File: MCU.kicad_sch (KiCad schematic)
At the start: 2 parts, among them U6 ESP32-S3-WROOM-1-N16R8, U9 M24C01-WMN

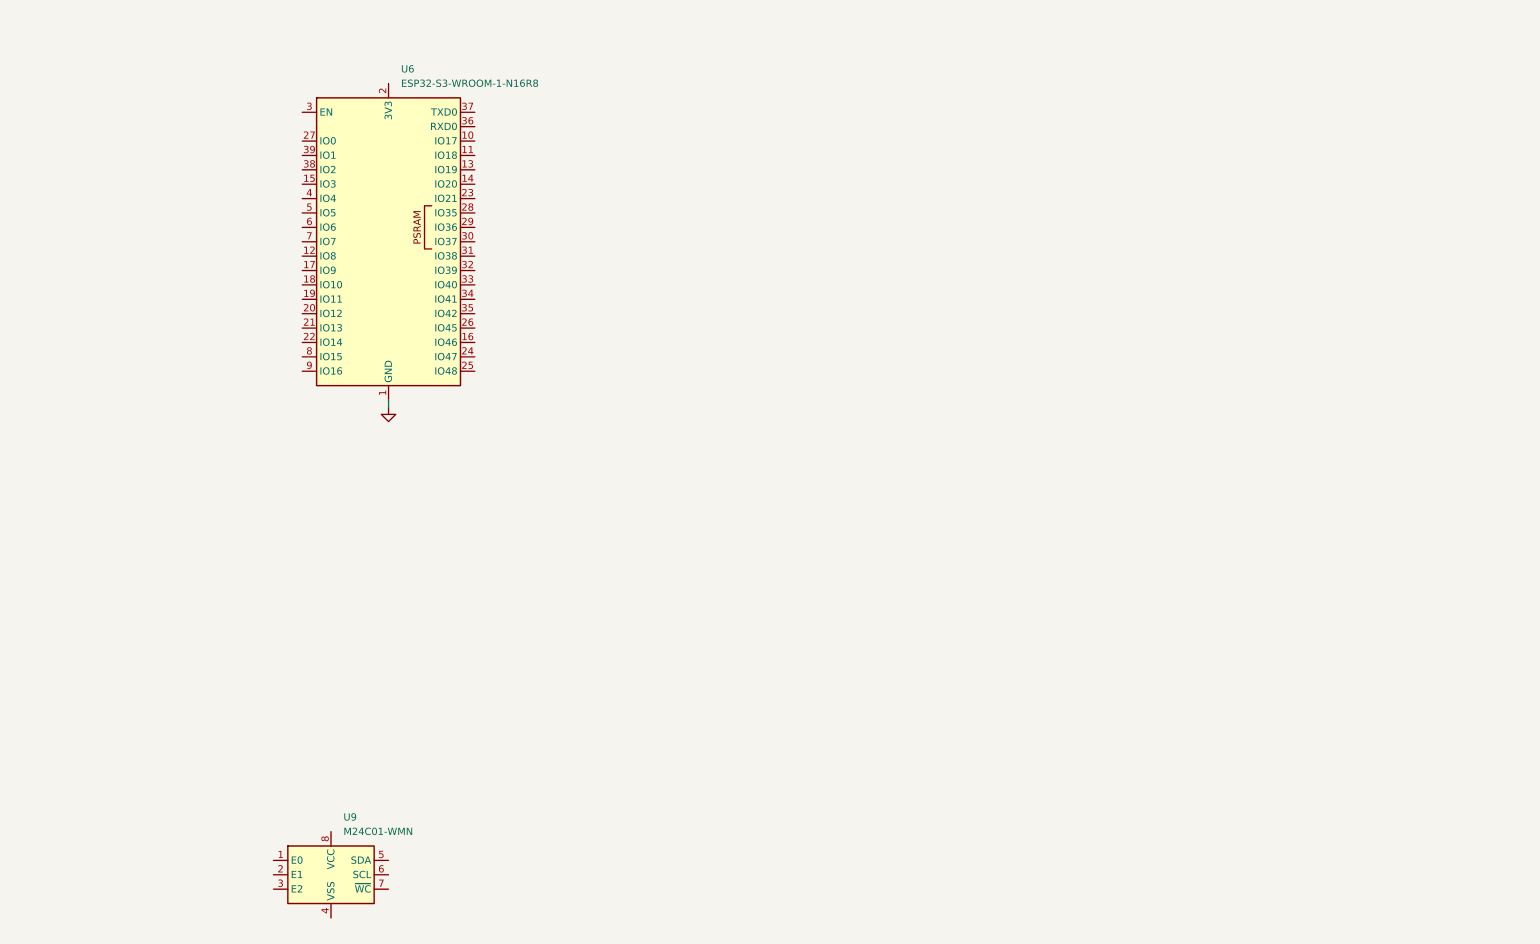
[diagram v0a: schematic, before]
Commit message: schematics mixer progress, mcu
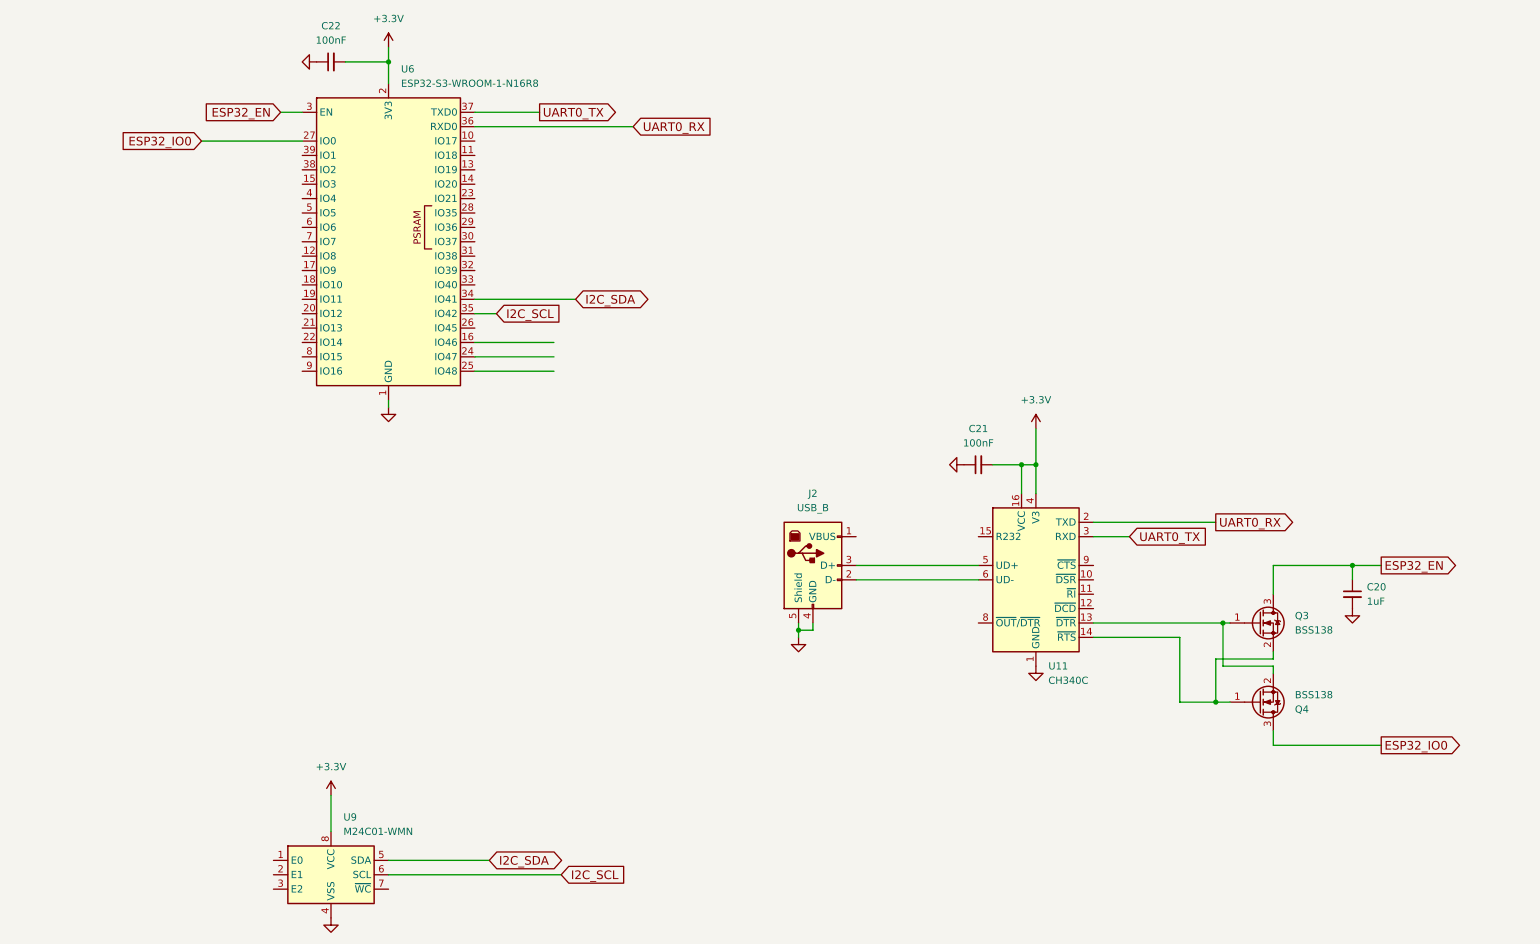
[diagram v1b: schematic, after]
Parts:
- added C20: 1uF, Capacitor_SMD:C_0603_1608Metric_Pad1.08x0.95mm_HandSolder, symbol Device:C_Small
- added C21, C22: 100nF, Capacitor_SMD:C_0603_1608Metric_Pad1.08x0.95mm_HandSolder, symbol Device:C_Small
- added J2: USB_B, Connector_USB:USB_B_OST_USB-B1HSxx_Horizontal, symbol Connector:USB_B
- added Q3, Q4: BSS138, Package_TO_SOT_SMD:SOT-23, symbol Transistor_FET:BSS138
- added U11: CH340C, Package_SO:SOIC-16_3.9x9.9mm_P1.27mm, symbol Interface_USB:CH340C
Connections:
- net GND: now also U9.4 (VSS), C20.2, C21.1, C22.1, J2.4 (GND), J2.5 (Shield), U11.1 (GND)
- net +3.3V: now reaches U6.2 (3V3)
- net +3.3V: now also U9.8 (VCC), C21.2, C22.2, U11.16 (VCC), U11.4 (V3)
- net ESP32_IO0: now reaches U6.27 (IO0)
- net ESP32_IO0: now also Q4.3 (D)
- net ESP32_EN: now reaches U6.3 (EN)
- net ESP32_EN: now also C20.1, Q3.3 (D)
- net I2C_SDA: now reaches U6.34 (IO41)
- net I2C_SDA: now also U9.5 (SDA)
- net I2C_SCL: now reaches U6.35 (IO42)
- net I2C_SCL: now also U9.6 (SCL)
- net UART0_RX: now reaches U6.36 (RXD0)
- net UART0_RX: now also U11.2 (TXD)
- net UART0_TX: now reaches U6.37 (TXD0)
- net UART0_TX: now also U11.3 (RXD)
- new net: Q3.2 (S), Q4.1 (G), U11.14 (~{RTS})
- new net: Q3.1 (G), Q4.2 (S), U11.13 (~{DTR})
- new net: J2.2 (D-), U11.6 (UD-)
- new net: J2.3 (D+), U11.5 (UD+)

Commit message: add BPF, add Firmware
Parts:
- added J3: Program_USB_JTAG, Connector_PinHeader_2.54mm:PinHeader_1x03_P2.54mm_Vertical, symbol Connector_Generic:Conn_01x03
- Q3: JLCPCB (none) -> C82045
- U11: JLCPCB (none) -> C7464026
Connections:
- net GND: now also U9.1 (E0), U9.2 (E1), U9.3 (E2), J3.3 (Pin_3)
- net I2C_SCL: now also U6.34 (IO41); no longer U6.35 (IO42)
- net I2C_SDA: now also U6.35 (IO42); no longer U6.34 (IO41)
- net KEYBOARD3: now reaches U6.12 (IO8)
- net USB_D-: now reaches U6.13 (IO19)
- net USB_D-: now also J3.1 (Pin_1)
- net USB_D+: now reaches U6.14 (IO20)
- net USB_D+: now also J3.2 (Pin_2)
- net LCD1602_IO3: now reaches U6.15 (IO3)
- net 74HC4053_RX_TX: now reaches U6.16 (IO46)
- net KEYBOARD4: now reaches U6.17 (IO9)
- net ENCODER_A: now reaches U6.18 (IO10)
- net ENCODER_B: now reaches U6.19 (IO11)
- net PREAMP: now reaches U6.24 (IO47)
- net EEPROM_WP: now reaches U6.25 (IO48)
- net EEPROM_WP: now also U9.7 (~{WC})
- net LCD1602_IO2: now reaches U6.38 (IO2)
- net LCD1602_IO1: now reaches U6.39 (IO1)
- net CW_Key_DOT: now reaches U6.4 (IO4)
- net CW_Key_DACH: now reaches U6.5 (IO5)
- net KEYBOARD1: now reaches U6.6 (IO6)
- net KEYBOARD2: now reaches U6.7 (IO7)

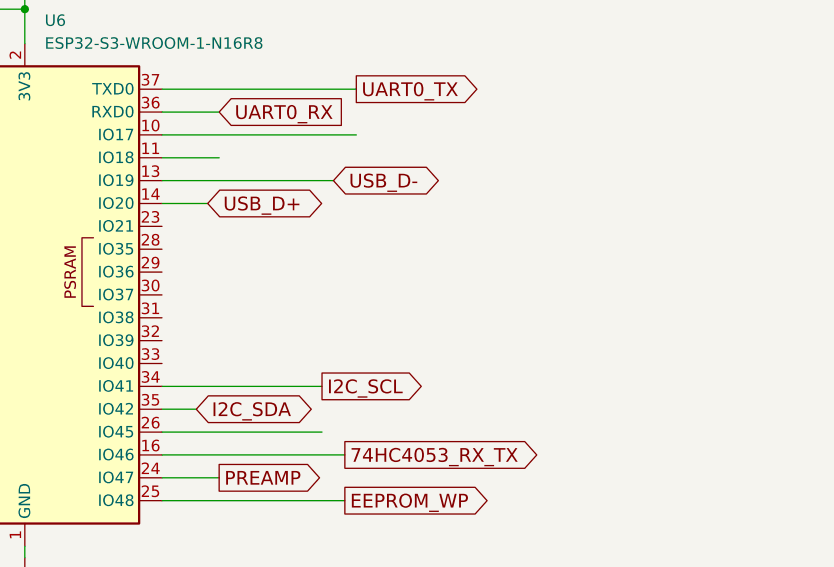
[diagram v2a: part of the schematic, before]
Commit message: add custom footprints, progress on schema and PCB
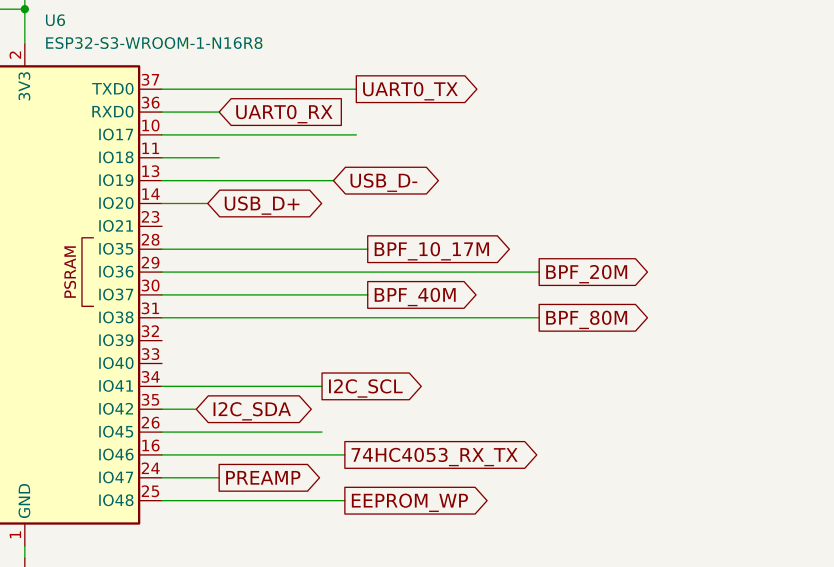
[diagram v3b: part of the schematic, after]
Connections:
- net BPF_10_17M: now reaches U6.28 (IO35)
- net BPF_20M: now reaches U6.29 (IO36)
- net BPF_40M: now reaches U6.30 (IO37)
- net BPF_80M: now reaches U6.31 (IO38)
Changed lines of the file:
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@@
+	(wire
+		(pts
+			(xy 95.25 60.96) (xy 118.11 60.96)
+		)
+		(stroke
+			(width 0)
+			(type default)
+		)
+	)
 	(wire
 		(pts
@@
 	(wire
 		(pts
+			(xy 95.25 63.5) (xy 137.16 63.5)
+		)
+		(stroke
+			(width 0)
+			(type default)
+		)
+	)
+	(wire
+		(pts
 			(xy 80.01 90.17) (xy 80.01 88.9)
 		)
@@
 	(wire
 		(pts
+			(xy 95.25 58.42) (xy 137.16 58.42)
+		)
+		(stroke
+			(width 0)
+			(type default)
+		)
+	)
+	(wire
+		(pts
 			(xy 80.01 29.21) (xy 80.01 33.02)
 		)
@@
 		(pts
 			(xy 236.22 149.86) (xy 255.27 149.86)
+		)
+		(stroke
+			(width 0)
+			(type default)
+		)
+	)
+	(wire
+		(pts
+			(xy 95.25 55.88) (xy 118.11 55.88)
 		)
 		(stroke
@@
 		)
 	)
+	(global_label "BPF_80M"
+		(shape output)
+		(at 137.16 63.5 0)
+		(fields_autoplaced yes)
+		(effects
+			(font
+				(size 1.524 1.524)
+			)
+			(justify left)
+		)
+		(property "Intersheetrefs" "${INTERSHEET_REFS}"
+			(at 150.1167 63.5 0)
+			(effects
+				(font
+					(size 1.27 1.27)
+				)
+				(justify left)
+				(hide yes)
+			)
+		)
+	)
 	(global_label "UART0_RX"
 		(shape output)
@@
 		)
 	)
+	(global_label "BPF_10_17M"
+		(shape output)
+		(at 118.11 55.88 0)
+		(fields_autoplaced yes)
+		(effects
+			(font
+				(size 1.524 1.524)
+			)
+			(justify left)
+		)
+		(property "Intersheetrefs" "${INTERSHEET_REFS}"
+			(at 135.1306 55.88 0)
+			(effects
+				(font
+					(size 1.27 1.27)
+				)
+				(justify left)
+				(hide yes)
+			)
+		)
+	)
 	(global_label "ESP32_EN"
 		(shape input)
@@
 		)
 	)
+	(global_label "BPF_40M"
+		(shape output)
+		(at 118.11 60.96 0)
+		(fields_autoplaced yes)
+		(effects
+			(font
+				(size 1.524 1.524)
+			)
+			(justify left)
+		)
+		(property "Intersheetrefs" "${INTERSHEET_REFS}"
+			(at 131.0667 60.96 0)
+			(effects
+				(font
+					(size 1.27 1.27)
+				)
+				(justify left)
+				(hide yes)
+			)
+		)
+	)
 	(global_label "74HC4053_RX_TX"
 		(shape output)
@@
 				(hide yes)
 			)
+		)
+	)
+	(global_label "BPF_20M"
+		(shape output)
+		(at 137.16 58.42 0)
+		(fields_autoplaced yes)
+		(effects
+			(font
+				(size 1.524 1.524)
+			)
+			(justify left)
+		)
+		(property "Intersheetrefs" "${INTERSHEET_REFS}"
+			(at 150.1167 58.42 0)
+			(effects
+				(font
+					(size 1.27 1.27)
+				)
+				(justify left)
+				(hide yes)
+			)

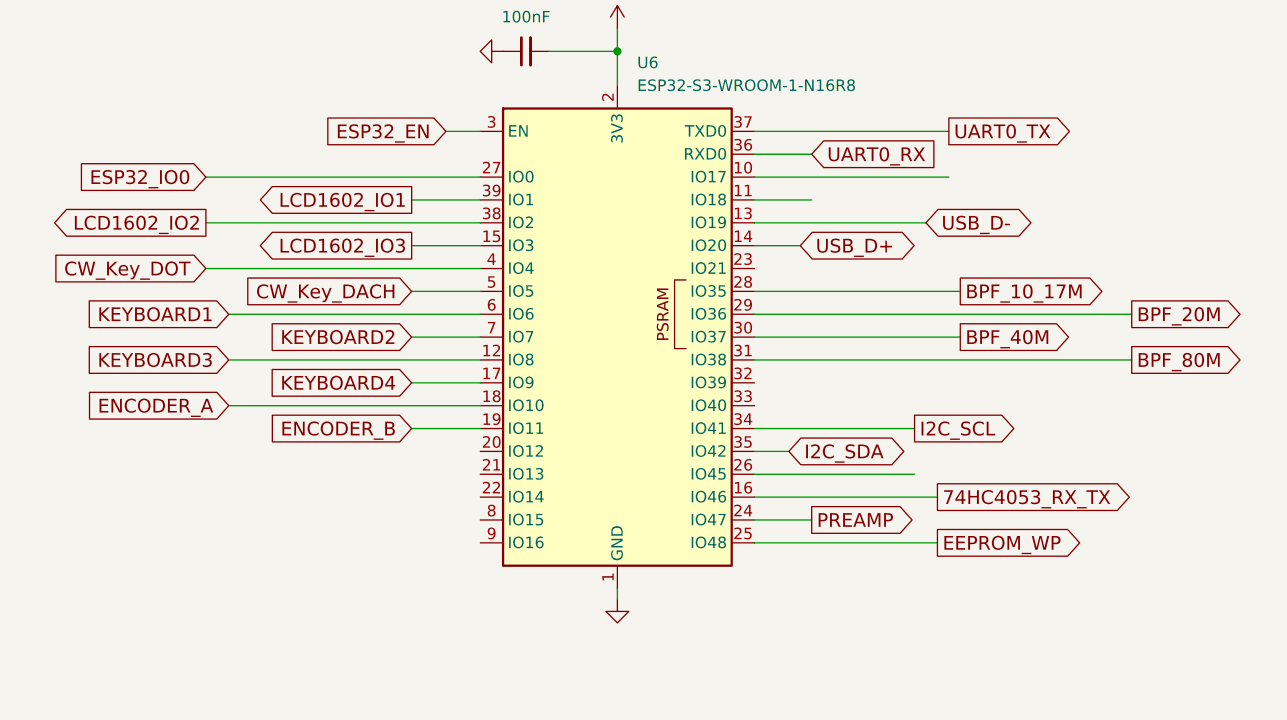
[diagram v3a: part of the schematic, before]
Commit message: progress in PCB, schematics some footprints are still missing
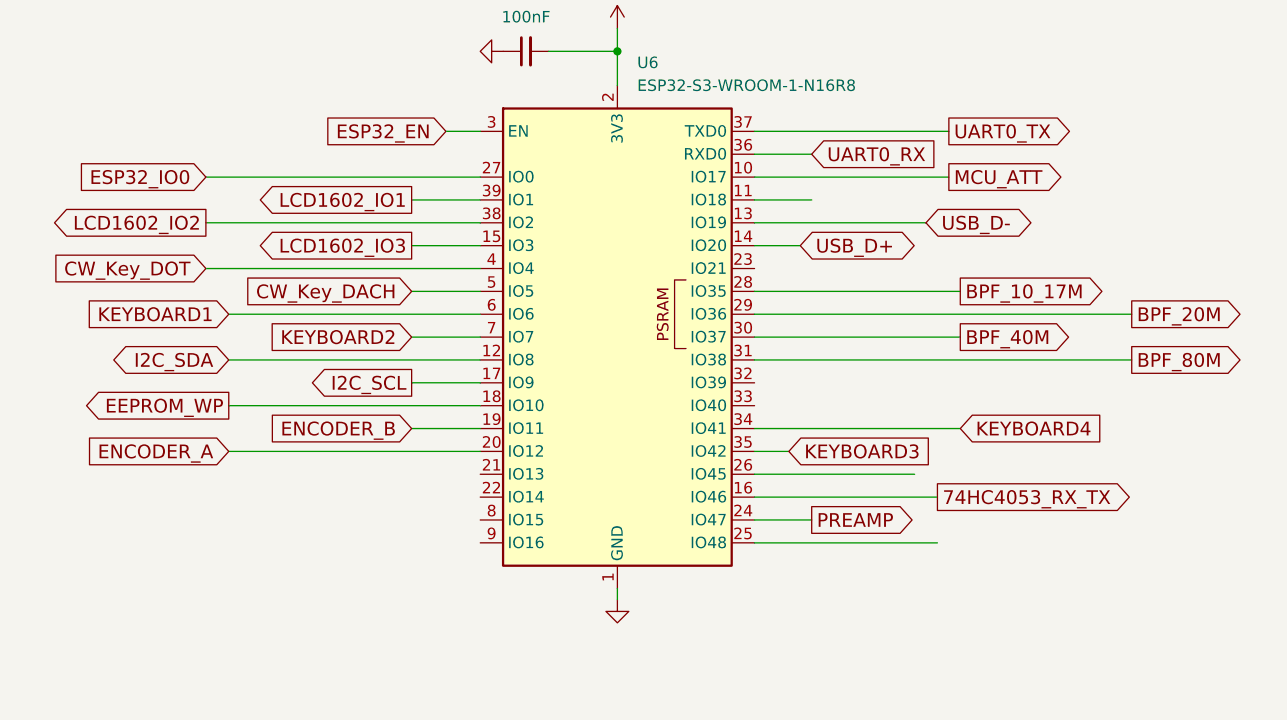
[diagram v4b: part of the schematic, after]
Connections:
- net EEPROM_WP: now also U6.18 (IO10); no longer U6.25 (IO48)
- net ENCODER_A: now also U6.20 (IO12); no longer U6.18 (IO10)
- net I2C_SCL: now also U6.17 (IO9); no longer U6.34 (IO41)
- net I2C_SDA: now also U6.12 (IO8); no longer U6.35 (IO42)
- net KEYBOARD3: now also U6.35 (IO42); no longer U6.12 (IO8)
- net KEYBOARD4: now also U6.34 (IO41); no longer U6.17 (IO9)
- net MCU_ATT: now reaches U6.10 (IO17)
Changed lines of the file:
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@@
+	(wire
+		(pts
+			(xy 36.83 73.66) (xy 64.77 73.66)
+		)
+		(stroke
+			(width 0)
+			(type default)
+		)
+	)
 	(wire
 		(pts
@@
 	(wire
 		(pts
-			(xy 95.25 71.12) (xy 113.03 71.12)
+			(xy 95.25 71.12) (xy 118.11 71.12)
 		)
 		(stroke
@@
 	(global_label "ENCODER_A"
 		(shape input)
-		(at 36.83 68.58 180)
-		(fields_autoplaced yes)
-		(effects
-			(font
-				(size 1.524 1.524)
-			)
-			(justify right)
-		)
-		(property "Intersheetrefs" "${INTERSHEET_REFS}"
-			(at 21.0428 68.58 0)
+		(at 36.83 73.66 180)
+		(fields_autoplaced yes)
+		(effects
+			(font
+				(size 1.524 1.524)
+			)
+			(justify right)
+		)
+		(property "Intersheetrefs" "${INTERSHEET_REFS}"
+			(at 21.0428 73.66 0)
 			(effects
 				(font
@@
 	(global_label "KEYBOARD4"
 		(shape input)
-		(at 57.15 66.04 180)
-		(fields_autoplaced yes)
-		(effects
-			(font
-				(size 1.524 1.524)
-			)
-			(justify right)
-		)
-		(property "Intersheetrefs" "${INTERSHEET_REFS}"
-			(at 41.2177 66.04 0)
-			(effects
-				(font
-					(size 1.27 1.27)
-				)
-				(justify right)
+		(at 118.11 71.12 0)
+		(fields_autoplaced yes)
+		(effects
+			(font
+				(size 1.524 1.524)
+			)
+			(justify left)
+		)
+		(property "Intersheetrefs" "${INTERSHEET_REFS}"
+			(at 134.0423 71.12 0)
+			(effects
+				(font
+					(size 1.27 1.27)
+				)
+				(justify left)
 				(hide yes)
 			)
@@
 	(global_label "I2C_SDA"
 		(shape bidirectional)
-		(at 99.06 73.66 0)
-		(fields_autoplaced yes)
-		(effects
-			(font
-				(size 1.524 1.524)
-			)
-			(justify left)
-		)
-		(property "Intersheetrefs" "${INTERSHEET_REFS}"
-			(at 112.1437 73.66 0)
-			(effects
-				(font
-					(size 1.27 1.27)
-				)
-				(justify left)
+		(at 36.83 63.5 180)
+		(fields_autoplaced yes)
+		(effects
+			(font
+				(size 1.524 1.524)
+			)
+			(justify right)
+		)
+		(property "Intersheetrefs" "${INTERSHEET_REFS}"
+			(at 23.7463 63.5 0)
+			(effects
+				(font
+					(size 1.27 1.27)
+				)
+				(justify right)
 				(hide yes)
 			)
@@
 	(global_label "KEYBOARD3"
 		(shape input)
-		(at 36.83 63.5 180)
-		(fields_autoplaced yes)
-		(effects
-			(font
-				(size 1.524 1.524)
-			)
-			(justify right)
-		)
-		(property "Intersheetrefs" "${INTERSHEET_REFS}"
-			(at 20.8977 63.5 0)
-			(effects
-				(font
-					(size 1.27 1.27)
-				)
-				(justify right)
+		(at 99.06 73.66 0)
+		(fields_autoplaced yes)
+		(effects
+			(font
+				(size 1.524 1.524)
+			)
+			(justify left)
+		)
+		(property "Intersheetrefs" "${INTERSHEET_REFS}"
+			(at 114.9923 73.66 0)
+			(effects
+				(font
+					(size 1.27 1.27)
+				)
+				(justify left)
 				(hide yes)
 			)
@@
 	(global_label "EEPROM_WP"
 		(shape output)
-		(at 115.57 83.82 0)
-		(fields_autoplaced yes)
-		(effects
-			(font
-				(size 1.524 1.524)
-			)
-			(justify left)
-		)
-		(property "Intersheetrefs" "${INTERSHEET_REFS}"
-			(at 131.9377 83.82 0)
-			(effects
-				(font
-					(size 1.27 1.27)
-				)
-				(justify left)
+		(at 36.83 68.58 180)
+		(fields_autoplaced yes)
+		(effects
+			(font
+				(size 1.524 1.524)
+			)
+			(justify right)
+		)
+		(property "Intersheetrefs" "${INTERSHEET_REFS}"
+			(at 20.4623 68.58 0)
+			(effects
+				(font
+					(size 1.27 1.27)
+				)
+				(justify right)
 				(hide yes)
 			)
@@
 	(global_label "I2C_SCL"
 		(shape output)
-		(at 113.03 71.12 0)
-		(fields_autoplaced yes)
-		(effects
-			(font
-				(size 1.524 1.524)
-			)
-			(justify left)
-		)
-		(property "Intersheetrefs" "${INTERSHEET_REFS}"
-			(at 124.8981 71.12 0)
-			(effects
-				(font
-					(size 1.27 1.27)
-				)
-				(justify left)
+		(at 57.15 66.04 180)
+		(fields_autoplaced yes)
+		(effects
+			(font
+				(size 1.524 1.524)
+			)
+			(justify right)
+		)
+		(property "Intersheetrefs" "${INTERSHEET_REFS}"
+			(at 45.2819 66.04 0)
+			(effects
+				(font
+					(size 1.27 1.27)
+				)
+				(justify right)
 				(hide yes)
 			)
@@
 			(effects
 				(font
+					(size 1.27 1.27)
+				)
+				(justify left)
+				(hide yes)
+			)
+		)
+	)
+	(global_label "MCU_ATT"
+		(shape output)
+		(at 116.84 43.18 0)
+		(fields_autoplaced yes)
+		(effects
+			(font
+				(size 1.524 1.524)
+			)
+			(justify left)
+		)
+		(property "Intersheetrefs" "${INTERSHEET_REFS}"
+			(at 129.2887 43.18 0)
+			(effects
+				(font
